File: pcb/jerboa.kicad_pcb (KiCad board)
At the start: 2 copper layers, 51.8 x 68.3 mm, 89 parts, among them IC1 SL18860DC, IC2 MAX-M8Q, IC3 Si4460, J1 CONN_01x02, J2 CONN_01x03, J3 CONN_01x02, J4 CONN_01x02, P1 SWD_TC, P2 COAX, P3 COAX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

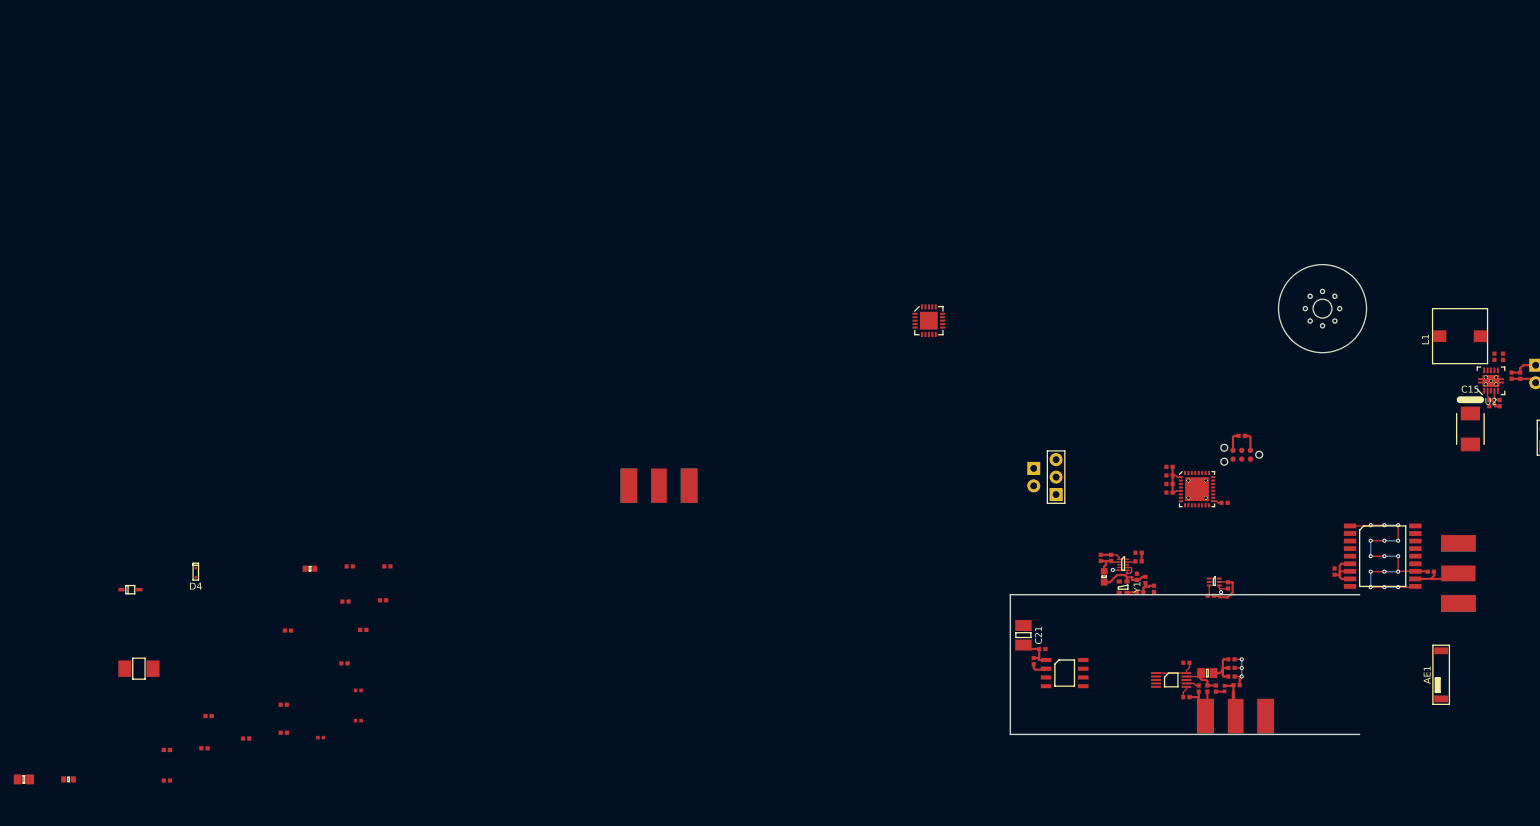
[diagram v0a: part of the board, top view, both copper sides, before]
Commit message: Redo si4460 matching for 169MHz
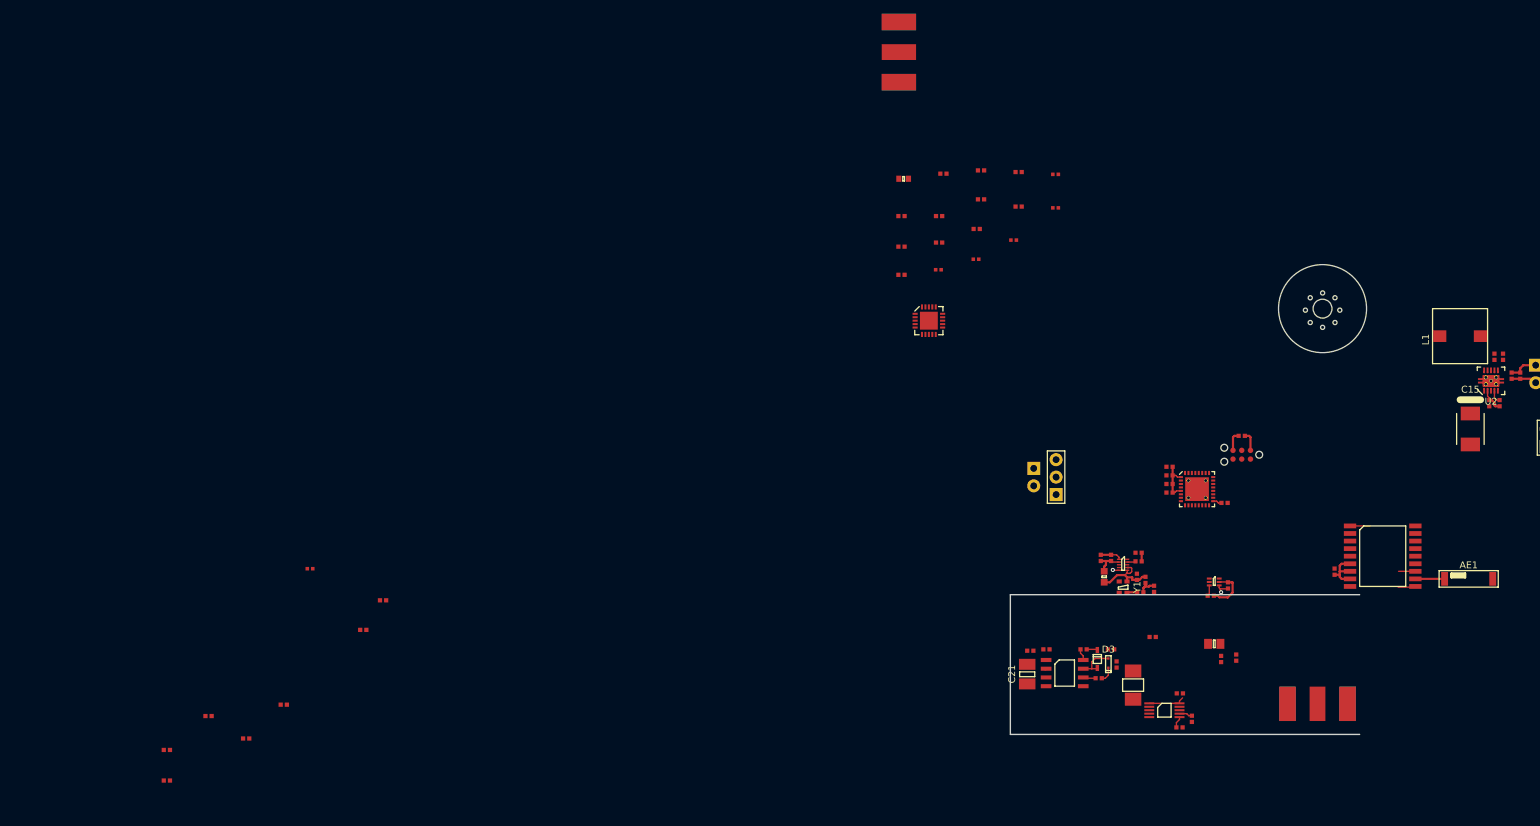
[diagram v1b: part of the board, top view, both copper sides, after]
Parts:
- removed C33, C36: 6.8pF, agg:0402
- removed C34: 2.2pF, agg:0402
- removed C35, C37, C38: 100nF, agg:0402
- removed D4: D_Capacitance, Jerboa:SC-79
- removed L4: 51nH, agg:0402-L
- removed L5: 39nH, agg:0603-L
- removed L6, L7: 18nH, agg:0402-L
- removed L8: 680nH, agg:0805
- removed L9: 43nH, agg:0402-L
- removed P4: COAX, agg:SMA-EDGE
- removed X3: MOUNT, agg:M2.5_MOUNT
- added C0: 39pF, agg:0402, F.Cu at (20.5, 23.8)
- added CC2: 470pF, agg:0402, F.Cu at (26.6, 17.6)
- added CM1: 6.8pF, agg:0402, F.Cu at (20.5, 28.2)
- added CM2: 18pF, agg:0402, F.Cu at (26.0, 23.8)
- added CM3: 18pF, agg:0402, F.Cu at (32.1, 17.1)
- added CP1: 3pF, agg:0402, F.Cu at (20.5, 32.3)
- added CP2: 2pF, agg:0402, F.Cu at (26.0, 27.6)
- added CR1: 12pF, agg:0402, F.Cu at (32.1, 21.4)
- added CR2: 6.2pF, agg:0402, F.Cu at (37.6, 17.4)
- added L0: 22nH, agg:0402, F.Cu at (31.5, 25.7)
- added LM1: 56nH, agg:0402-L, F.Cu at (25.9, 31.6)
- added LM2: 47nH, agg:0402-L, F.Cu at (31.4, 30.1)
- added LM3: 68nH, agg:0402-L, F.Cu at (36.8, 27.3)
- added LM4: 47nH, agg:0402-L, F.Cu at (42.9, 22.6)
- added LR1: 220nH, agg:0402, F.Cu at (37.6, 22.4)
- added LR2: 150nH, agg:0402-L, F.Cu at (42.9, 17.7)
- added Lchoke1: 470nH, agg:0603-L, F.Cu at (20.8, 18.4)
- added X1: MOUNT, agg:M2.5_MOUNT, F.Cu at (81.8, 37.5)
- C26: value 3.9pF -> 100nF
- C27: value 100nF -> 1.2pF
- C28: value 15pF -> 2.2pF
- C29: value 2.2pF -> 100nF
- C30: value 8.2pF -> 6.8pF
- C31: value 15pF -> 100nF
- C32: value 1.2pF -> 100nF
- D2: value ESD_DIODE -> D_Capacitance; footprint agg:0402 -> agg:SOD-323
- D3: footprint agg:SOD-323 -> Jerboa:SC-79
- L2: value 56nH -> 680nH
- L3: value 220nH -> 43nH; footprint agg:0603-L -> agg:0402-L
- moved L2 174.2 mm to (66.0, 86.0)
- moved Y2 144.6 mm to (54.2, 92.0), turned to 90 degrees
- moved D3 142.6 mm to (50.6, 88.8), turned to 180 degrees
- moved C22 132.6 mm to (51.0, 86.8)
- moved C24 125.7 mm to (57.0, 85.0), turned to 180 degrees
- moved C26 122.1 mm to (61.0, 93.2)
- moved R15 118.8 mm to (49.2, 91.0)
- moved C23 112.5 mm to (51.8, 89.0), turned to 90 degrees
- moved P2 111.2 mm to (20.1, -0.06)
- moved R14 107.5 mm to (47.0, 86.8)
- moved P3 100.9 mm to (81.0, 94.7)
- moved D2 50.1 mm to (49.0, 88.2), turned to 270 degrees
- moved AE1 14.5 mm to (103.0, 76.5), turned to 180 degrees
- moved C32 6.16 mm to (69.2, 88.0)
- moved C21 5.68 mm to (38.8, 90.4), turned to 270 degrees
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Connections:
- C26 pad 1: /radio/RADIO_RXp -> GND
- C26 pad 2: GND -> 3v3
- C27 pad 2: 3v3 -> Net-(C27-Pad2)
- C28 pad 1: /radio/RADIO_TX -> Net-(C27-Pad2)
- C29 pad 1: /radio/RADIO_RXn -> Net-(C29-Pad1)
- C29 pad 2: Net-(C29-Pad2) -> GND
- C30 pad 1: Net-(C29-Pad2) -> Net-(C30-Pad1)
- C31 pad 1: Net-(C31-Pad1) -> Net-(C29-Pad1)
- C32 pad 1: GND -> Net-(C29-Pad1)
- C32 pad 2: Net-(C32-Pad2) -> GND
- D2 pad 1: Net-(AE1-Pad2) -> Net-(C22-Pad1)
- D3 pad 1: Net-(C22-Pad1) -> Net-(C23-Pad1)
- L2 pad 1: /radio/RADIO_RXn -> Net-(C29-Pad1)
- L2 pad 2: /radio/RADIO_RXp -> Net-(C27-Pad2)
- L3 pad 1: 3v3 -> Net-(C30-Pad1)
- L3 pad 2: /radio/RADIO_TX -> Net-(C28-Pad2)
- P2 pad 1: Net-(AE1-Pad2) -> Net-(CC2-Pad2)
- P3 pad 1: Net-(C33-Pad1) -> Net-(C30-Pad1)
- U5 pad 9: Net-(C32-Pad2) -> Net-(C27-Pad2)
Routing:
- net GND: track 67.8 -> 26.4 mm, vias 20 -> 2
- net 3v3: track 50.5 -> 43.9 mm
- net Net-(C35-Pad1): track 6.53 -> 0.00 mm
- net Net-(C32-Pad2): track 6.20 -> 0.00 mm
- net Net-(C36-Pad1): track 5.98 -> 0.00 mm
- net Net-(AE1-Pad2): track 7.91 -> 4.25 mm
- net /DAC_NCS: track 2.51 -> 0.19 mm
- net Net-(C23-Pad1): track 0.00 -> 2.22 mm
- net /radio/FINE: track 0.00 -> 1.85 mm
- net /radio/COARSE: track 0.00 -> 1.71 mm
- net Net-(C22-Pad1): track 0.00 -> 1.59 mm
- net Net-(C34-Pad2): track 1.27 -> 0.00 mm
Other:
- net class Default: via_dia 0.6 -> 0.8; via_drill 0.3 -> 0.4
- net class Power: via_dia 0.6 -> 0.8; via_drill 0.3 -> 0.4
- net class Tight: via_dia 0.6 -> 0.8; via_drill 0.3 -> 0.4
- rule trace_min: 0.2 -> 0.15
- rule via_min_drill: 0.3 -> 0.4
- rule via_min_size: 0.4 -> 0.8

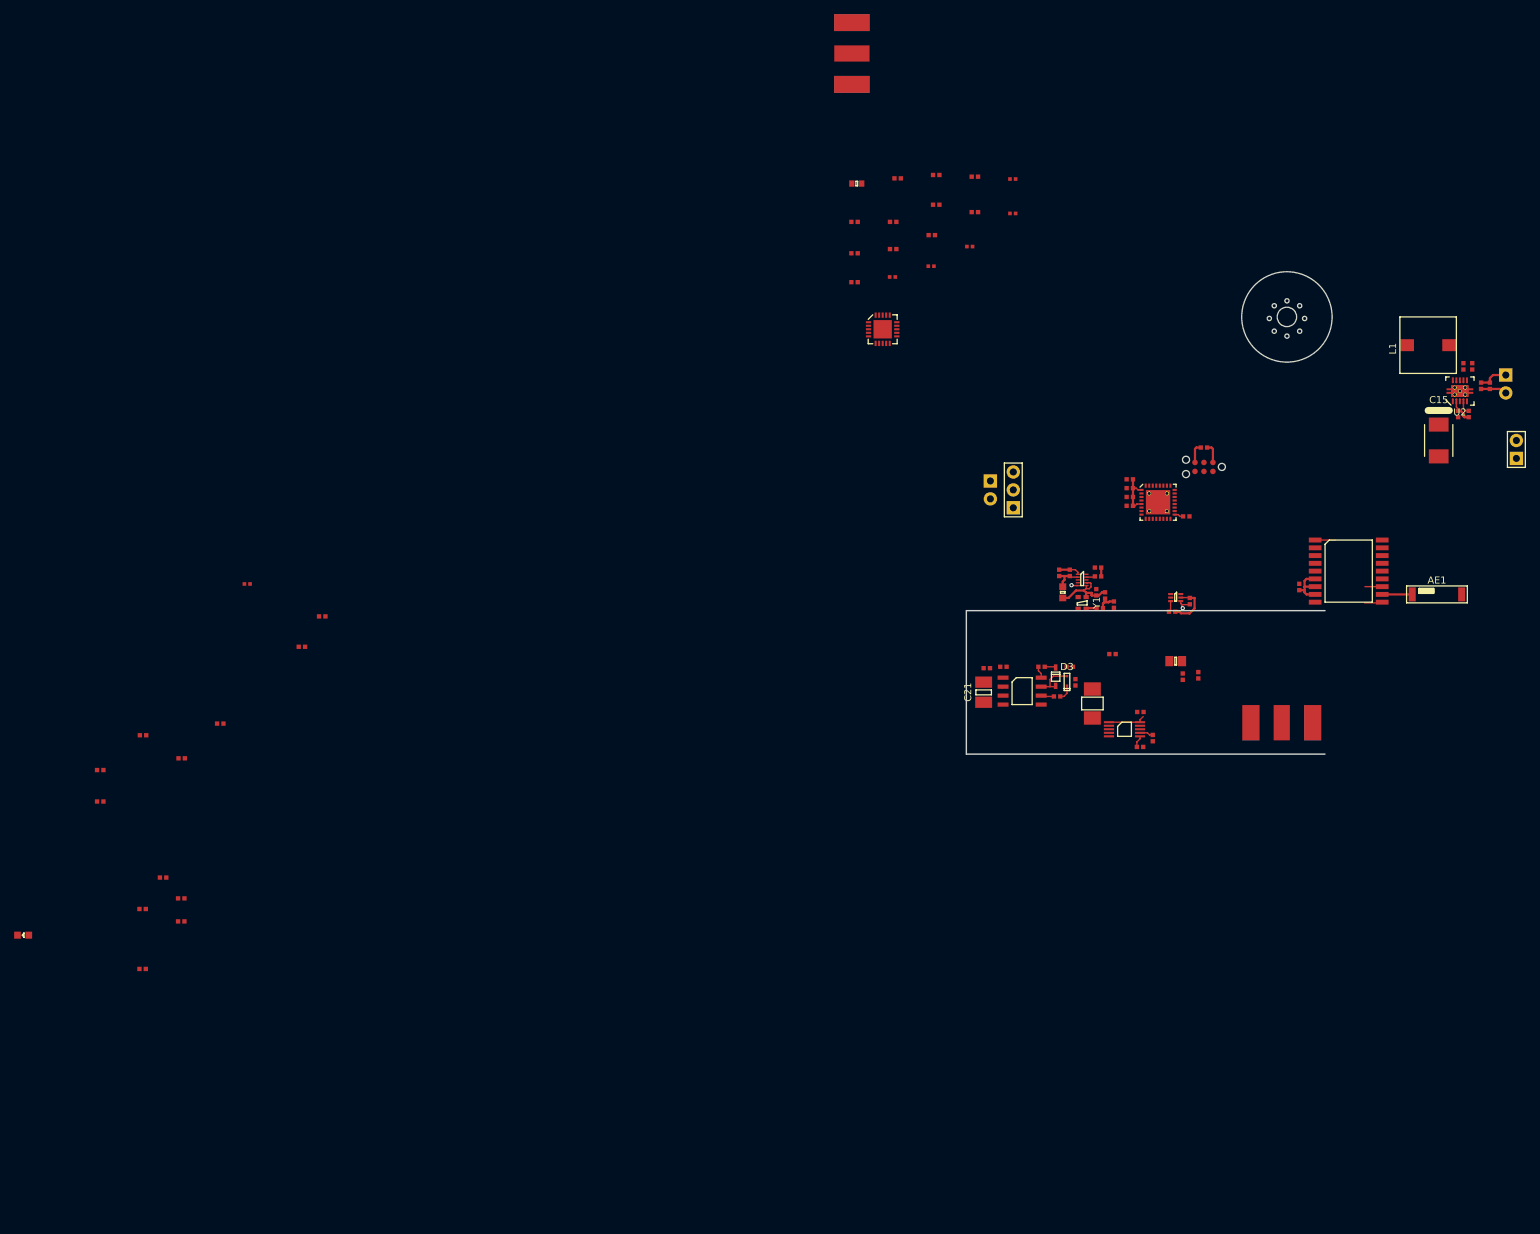
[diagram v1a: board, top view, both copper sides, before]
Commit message: WIP: work on pcb, use guitar wire ground plane antenna and remove rx matching on si4460 as there is nothing to receive
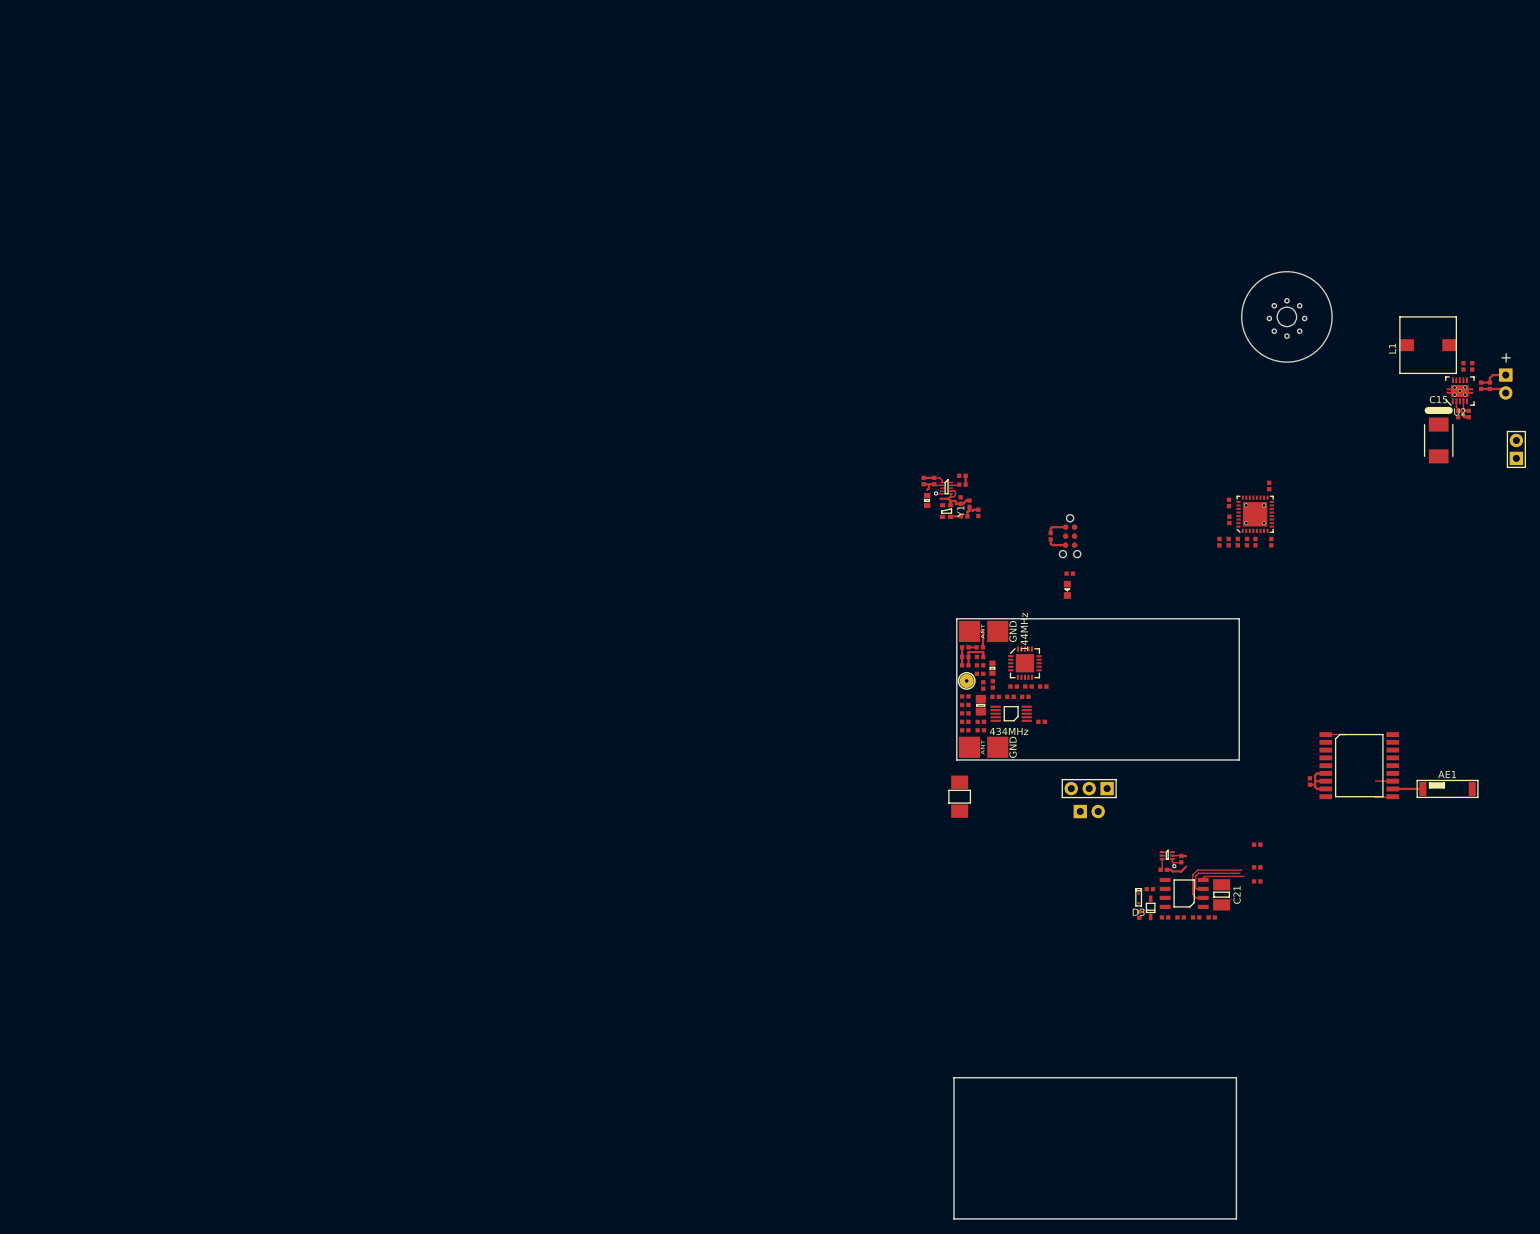
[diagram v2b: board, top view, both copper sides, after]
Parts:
- removed CR1: 12pF, agg:0402
- removed CR2: 6.2pF, agg:0402
- removed LR1: 220nH, agg:0402
- removed LR2: 150nH, agg:0402-L
- added TP1: TESTPAD, Jerboa:ANT_GND_PASSTHROUGH, F.Cu at (36.4, 88.8)
- L3, LM1, LM2, LM3, LM4: footprint agg:0402-L -> agg:0402
- P2: value COAX -> 144MHz; footprint agg:SMA-EDGE -> Jerboa:GND_PLANE_ANT
- P3: value COAX -> 434MHz; footprint agg:SMA-EDGE -> Jerboa:GND_PLANE_ANT
- R3: footprint agg:0603 -> agg:0603-L
- moved C10 164.8 mm to (76.1, 69.2), turned to 270 degrees
- moved R9 164.0 mm to (79.5, 69.2), turned to 270 degrees
- moved R7 159.0 mm to (73.6, 66.0), turned to 90 degrees
- moved R8 158.6 mm to (73.5, 63.6), turned to 90 degrees
- moved D1 155.8 mm to (50.6, 75.9), turned to 90 degrees
- moved R6 142.8 mm to (51.0, 73.6), turned to 180 degrees
- moved C28 125.2 mm to (38.4, 94.6)
- moved C30 122.6 mm to (36.2, 95.8), turned to 180 degrees
- moved C18 120.4 mm to (45.1, 89.6), turned to 180 degrees
- moved C31 116.5 mm to (36.2, 92.2), turned to 180 degrees
- moved CM3 109.9 mm to (77.5, 117.2), turned to 180 degrees
- moved L3 105.9 mm to (38.4, 95.8)
- moved C29 105.6 mm to (36.2, 91.0), turned to 180 degrees
- moved C19 105.2 mm to (47.2, 89.6), turned to 180 degrees
- moved CM2 102.2 mm to (77.5, 112.0)
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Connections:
- IC3 pad 2: /radio/RADIO_RXp -> /radio/RADIO_RXn
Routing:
- net 3v3: track 43.9 -> 27.1 mm
- net /DAC_NCS: track 0.19 -> 12.3 mm
- net /MCU_SCK: track 0.00 -> 9.74 mm
- net /MCU_MOSI: track 0.00 -> 6.65 mm
- net GND: track 26.4 -> 20.7 mm
- net Net-(CM2-Pad1): track 0.00 -> 4.60 mm
- net Net-(CC2-Pad2): track 0.00 -> 4.10 mm
- net Net-(CM3-Pad1): track 0.00 -> 2.55 mm
- net Net-(C23-Pad1): track 2.22 -> 0.00 mm
- net /MICRF_EN: track 1.92 -> 0.00 mm
- net /radio/FINE: track 1.85 -> 0.00 mm
- net /radio/COARSE: track 1.71 -> 0.00 mm
- net Net-(R17-Pad1): track 1.69 -> 0.00 mm
- net Net-(C22-Pad1): track 1.59 -> 0.00 mm
- net Net-(CC2-Pad1): track 0.00 -> 1.15 mm
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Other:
- board size 51.8 x 68.3 mm -> 53.6 x 134.2 mm
- board text added: "+"
- board text added: "ANT GND"
